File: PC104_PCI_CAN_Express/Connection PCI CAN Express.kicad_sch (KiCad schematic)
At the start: 2 parts

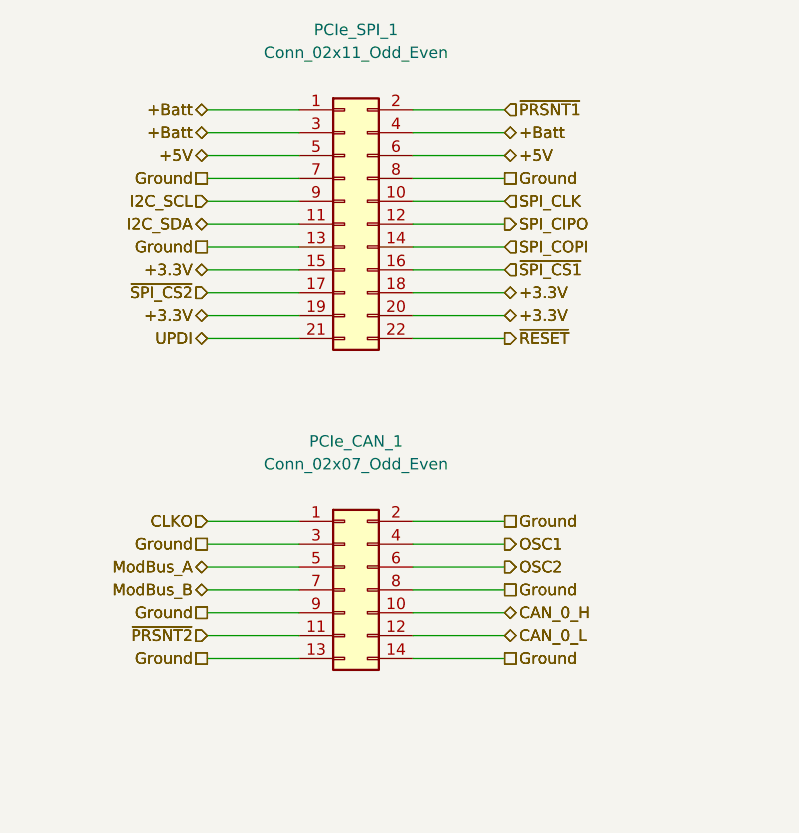
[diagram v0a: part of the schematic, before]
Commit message: Adding : licence file for CC-BY-SA-4.0
Update :
- PC104_PCI_CAN_Express -> PCB silkscreen
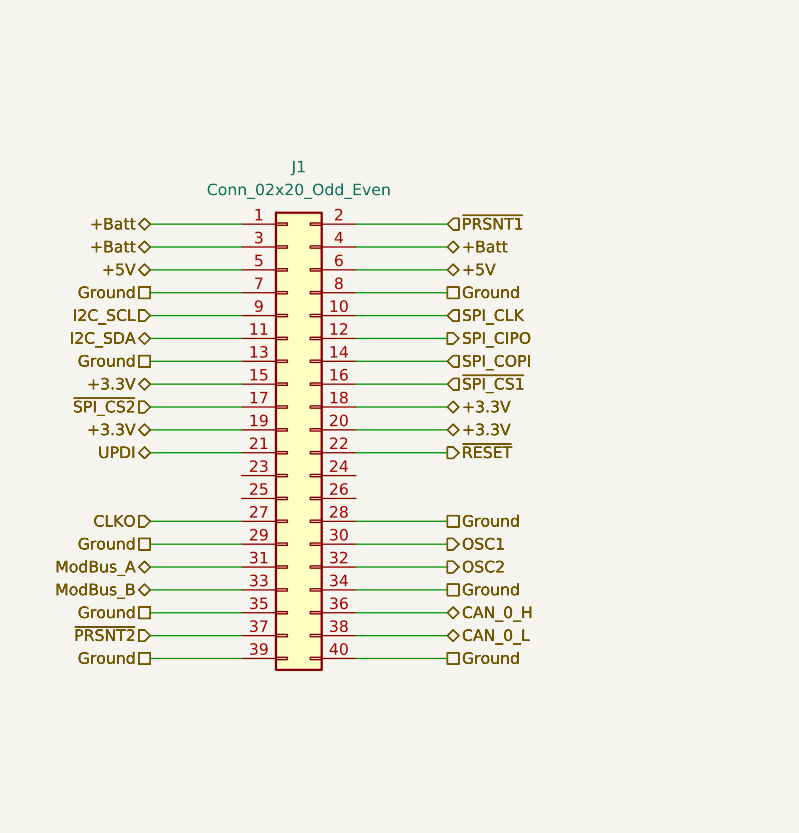
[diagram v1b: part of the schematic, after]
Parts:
- removed PCIe_CAN_1: Conn_02x07_Odd_Even, Connector_PinHeader_2.54mm:PinHeader_2x07_P2.54mm_Vertical, symbol Connector_Generic:Conn_02x07_Odd_Even
- removed PCIe_SPI_1: Conn_02x11_Odd_Even, Connector_PinHeader_2.54mm:PinHeader_2x11_P2.54mm_Vertical, symbol Connector_Generic:Conn_02x11_Odd_Even
- added J1: Conn_02x20_Odd_Even, Connector_IDC:IDC-Header_2x20_P2.54mm_Vertical, symbol Connector_Generic:Conn_02x20_Odd_Even
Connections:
- net +3.3V: now also J1.15 (Pin_15), J1.18 (Pin_18), J1.19 (Pin_19), J1.20 (Pin_20)
- net +5V: now also J1.5 (Pin_5), J1.6 (Pin_6)
- net +Batt: now also J1.1 (Pin_1), J1.3 (Pin_3), J1.4 (Pin_4)
- net CAN_0_H: now also J1.36 (Pin_36)
- net CAN_0_L: now also J1.38 (Pin_38)
- net CLKO: now also J1.27 (Pin_27)
- net Ground: now also J1.13 (Pin_13), J1.28 (Pin_28), J1.29 (Pin_29), J1.34 (Pin_34), J1.35 (Pin_35), J1.39 (Pin_39), J1.40 (Pin_40), J1.7 (Pin_7), J1.8 (Pin_8)
- net I2C_SCL: now also J1.9 (Pin_9)
- net I2C_SDA: now also J1.11 (Pin_11)
- net ModBus_A: now also J1.31 (Pin_31)
- net ModBus_B: now also J1.33 (Pin_33)
- net OSC1: now also J1.30 (Pin_30)
- net OSC2: now also J1.32 (Pin_32)
- net SPI_CIPO: now also J1.12 (Pin_12)
- net SPI_CLK: now also J1.10 (Pin_10)
- net SPI_COPI: now also J1.14 (Pin_14)
- net UPDI: now also J1.21 (Pin_21)
- net ~{PRSNT1}: now also J1.2 (Pin_2)
- net ~{PRSNT2}: now also J1.37 (Pin_37)
- net ~{RESET}: now also J1.22 (Pin_22)
- net ~{SPI_CS1}: now also J1.16 (Pin_16)
- net ~{SPI_CS2}: now also J1.17 (Pin_17)
